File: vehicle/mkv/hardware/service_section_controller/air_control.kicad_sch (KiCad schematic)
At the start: 25 parts

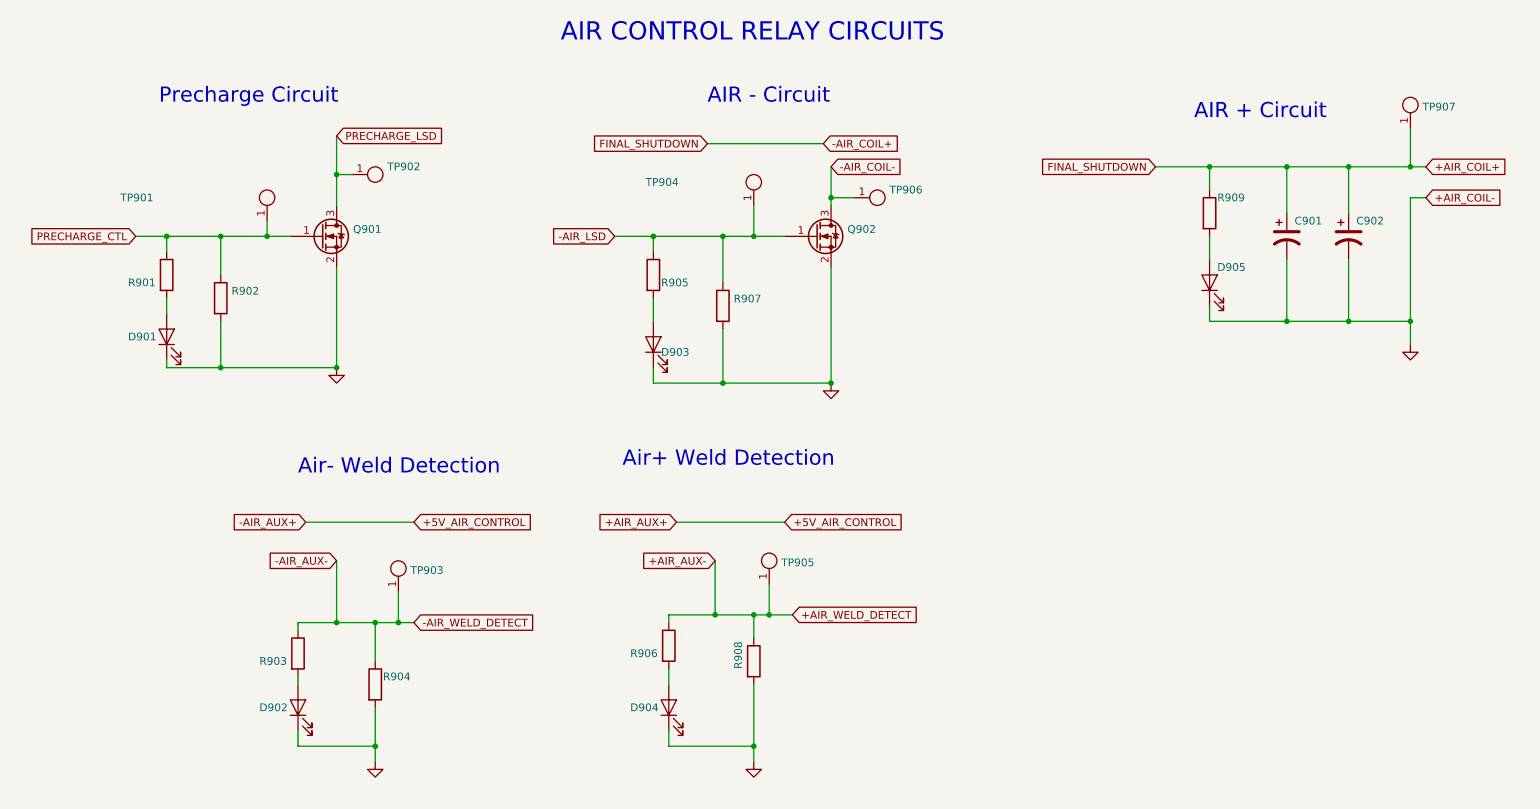
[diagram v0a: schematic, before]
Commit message: chore: annotate migrated schematics
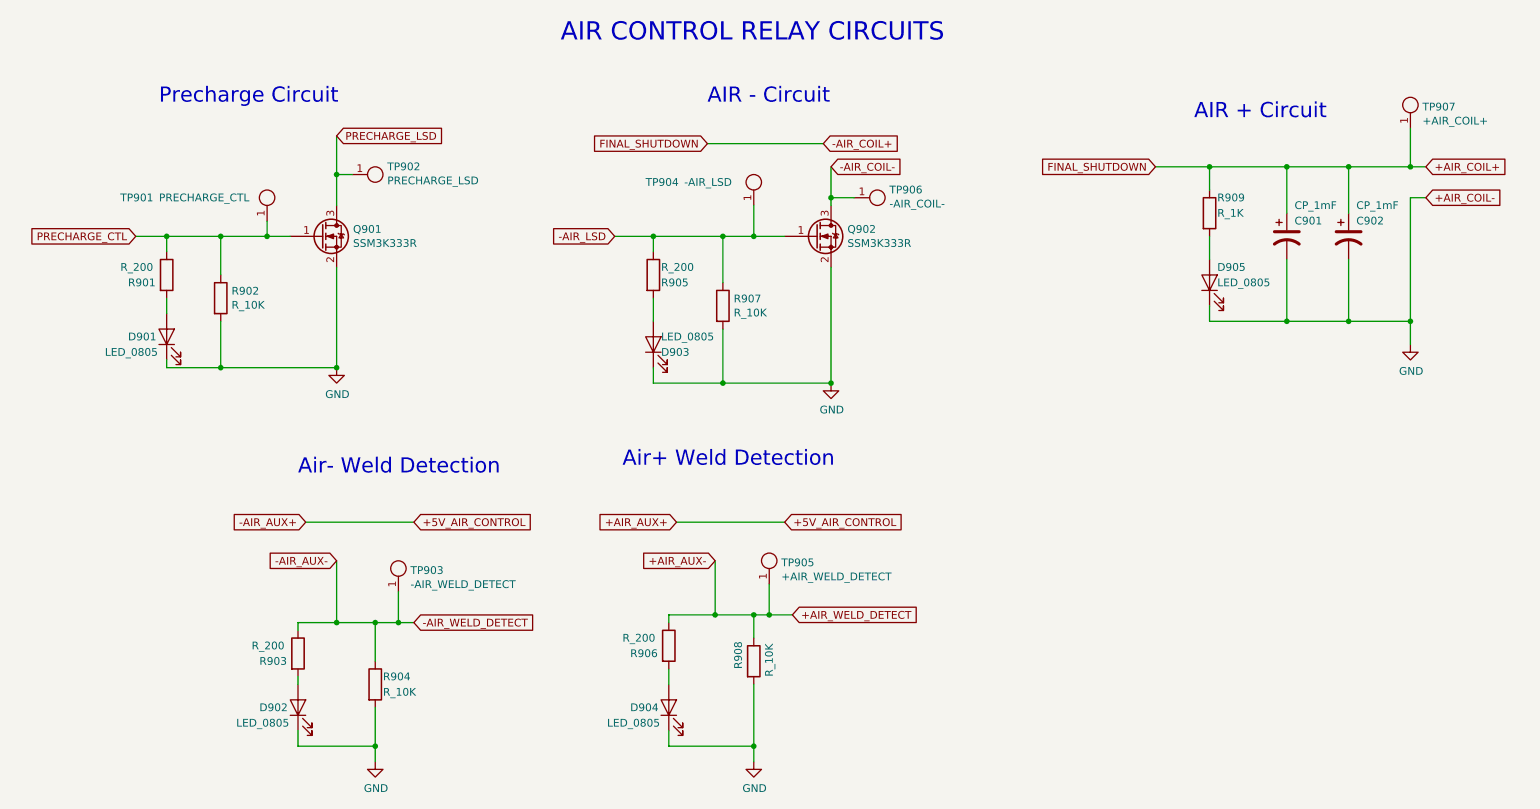
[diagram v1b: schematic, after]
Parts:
- C901, C902: value (none) -> CP_1mF; footprint (none) -> footprints:C_Radial_D10_L13_P5_OEM
- D901, D902, D903, D904, D905: value (none) -> LED_0805; footprint (none) -> footprints:LED_0805_OEM
- Q901, Q902: value (none) -> SSM3K333R; footprint (none) -> footprints:SOT-23F
- R901, R903, R905, R906: value (none) -> R_200; footprint (none) -> footprints:R_0805_OEM
- R902, R904, R907, R908: value (none) -> R_10K; footprint (none) -> footprints:R_0805_OEM
- R909: value (none) -> R_1K; footprint (none) -> footprints:R_0805_OEM
- TP901: value (none) -> PRECHARGE_CTL; footprint (none) -> TestPoint:TestPoint_Pad_D1.0mm
- TP902: value (none) -> PRECHARGE_LSD; footprint (none) -> TestPoint:TestPoint_Pad_D1.0mm
- TP903: value (none) -> -AIR_WELD_DETECT; footprint (none) -> TestPoint:TestPoint_Pad_D1.0mm
- TP904: value (none) -> -AIR_LSD; footprint (none) -> TestPoint:TestPoint_Pad_D1.0mm
- TP905: value (none) -> +AIR_WELD_DETECT; footprint (none) -> TestPoint:TestPoint_Pad_D1.0mm
- TP906: value (none) -> -AIR_COIL-; footprint (none) -> TestPoint:TestPoint_Pad_D1.0mm
- TP907: value (none) -> +AIR_COIL+; footprint (none) -> TestPoint:TestPoint_Pad_D1.0mm
